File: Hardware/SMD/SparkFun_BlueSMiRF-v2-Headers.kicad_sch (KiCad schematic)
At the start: 38 parts, among them J1 Conn_01x06, Q1 NMOS_0.2A_50V, Q2 NMOS_0.2A_50V, SW1 SPST_Momentary_4.6x2.8mm, U1 ESP32-PICO-V3-02, U2 AP2112K-3.3

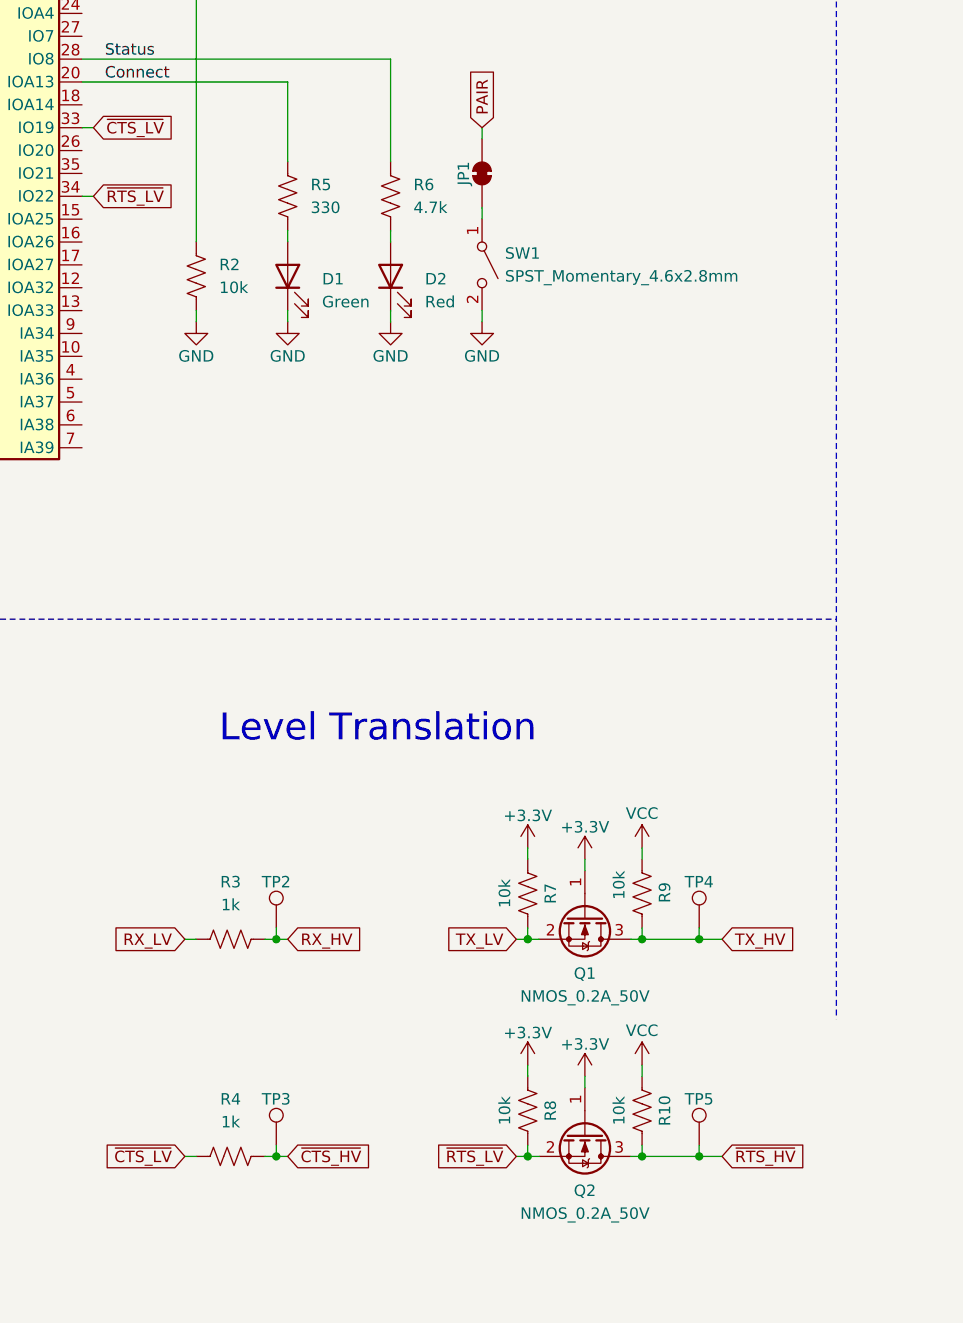
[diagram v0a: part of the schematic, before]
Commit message: Add 3D models
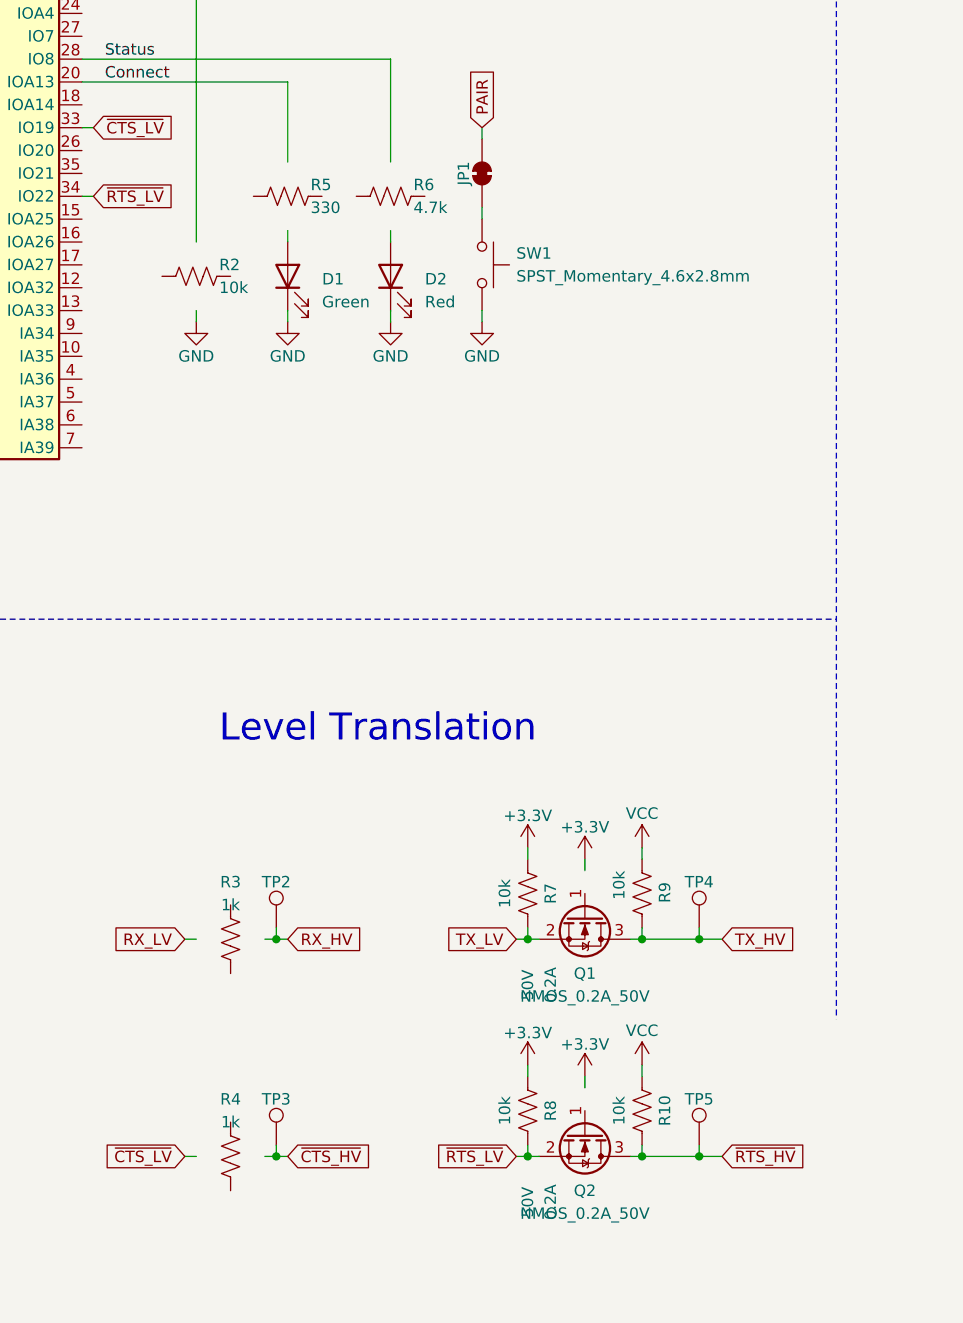
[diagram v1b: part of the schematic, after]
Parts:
- D1: footprint SparkFun-LED:LED_0603_1608Metric -> SparkFun-LED:LED_0603_1608Metric_Green
- D2: footprint SparkFun-LED:LED_0603_1608Metric -> SparkFun-LED:LED_0603_1608Metric_Red
- J1: footprint SparkFun-Connector:1X06-SMD_RA_MALE -> SparkFun-Connector:1x06_SMD_RA_Male
- JP1: footprint SparkFun-Jumper:SMT-JUMPER_2_NC_TRACE_SILK -> SparkFun-Jumper:Jumper_2_NC_Trace
- JP2: footprint SparkFun-Jumper:SMT-JUMPER_2_NO_SILK -> SparkFun-Jumper:Jumper_2_NO
- Q1, Q2: IMax (none) -> 0.2A; VMax (none) -> 50V
- SW1: footprint SparkFun-Switch:Momentary_SMD_4.6x2.8mm -> SparkFun-Switch:Push_SMD_4.6x2.8mm_h2.5mm; symbol SparkFun-Switch:SPST_Momentary_4.6x2.8mm -> SparkFun-Switch:SPST_Push_SMD_4.6x2.8mm_h2.5mm
- TP1: footprint SparkFun-Connector:1X01 -> SparkFun-Connector:1x01
- U1: footprint SparkFun-RF:ESP32-MINI -> SparkFun-RF:ESP32-PICO-MINI
- U2: Imax (none) -> 600mA; Iq (none) -> 55µA; VMax (none) -> 6V
- U3: footprint SparkFun-Aesthetic:ORDERING_INSTRUCTIONS -> SparkFun-Aesthetic:Ordering_Instructions
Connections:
- net +3.3V: no longer Q1.1 (G), Q2.1 (G)
- net Connect: no longer R5.1
- net GND: no longer R2.2
- net RX_HV: no longer R3.2
- net RX_LV: no longer R3.1
- net Status: no longer R6.1
- net ~{CTS_HV}: no longer R4.2
- net ~{CTS_LV}: no longer R4.1
- net at D1.2 (A): no longer R5.2
- net at U1.21 (IOA15): no longer R2.1
- net at R6.2: no longer D2.2 (A)

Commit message: Revert "Add 3D models"
This reverts commit f06ec004f059f8b2f723d6c27b798dd6a6ac20d5.
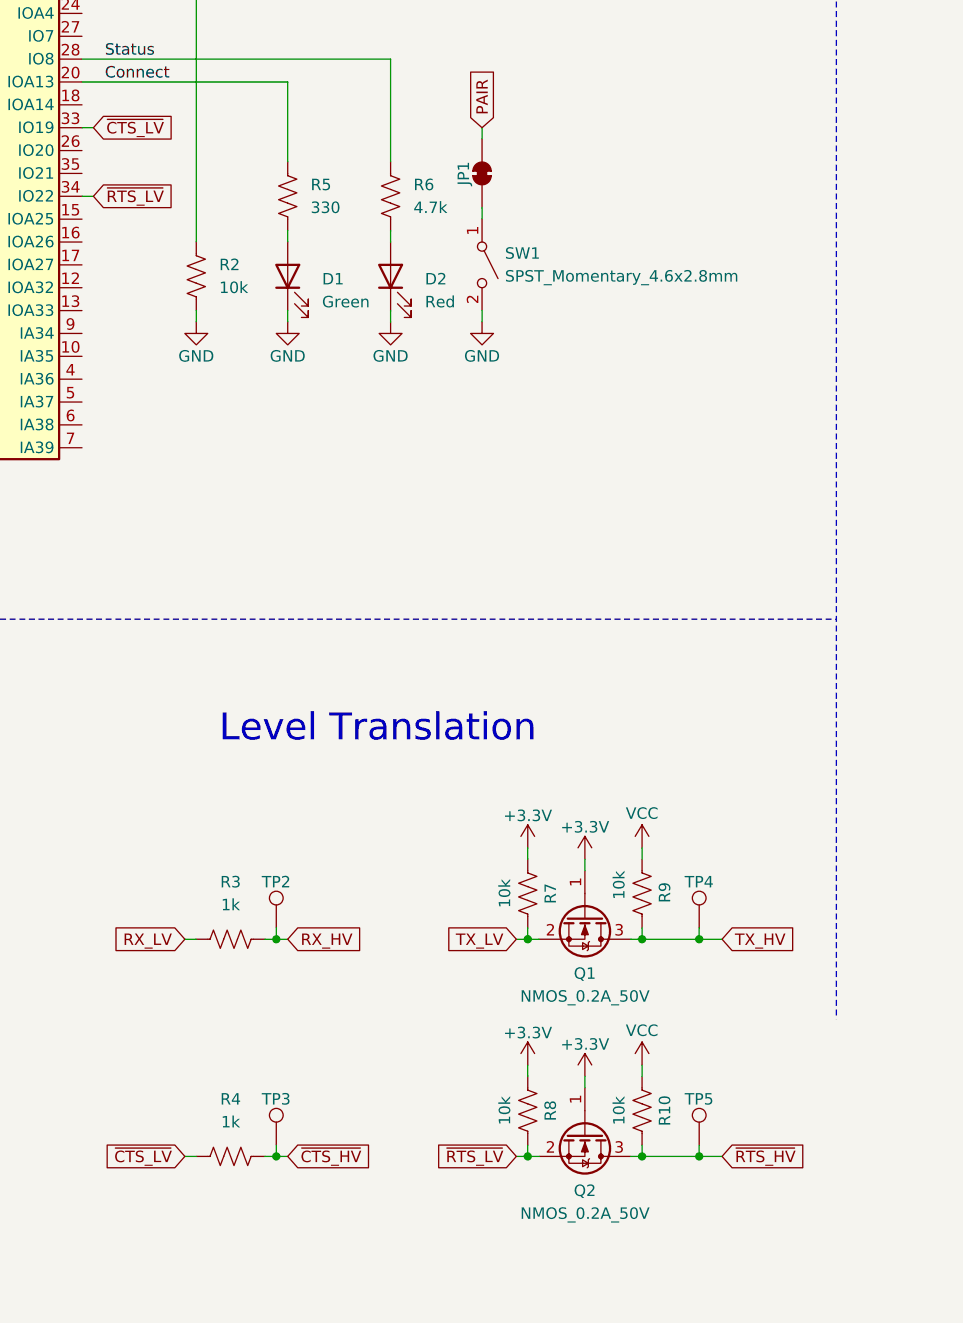
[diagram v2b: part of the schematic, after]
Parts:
- D1: footprint SparkFun-LED:LED_0603_1608Metric_Green -> SparkFun-LED:LED_0603_1608Metric
- D2: footprint SparkFun-LED:LED_0603_1608Metric_Red -> SparkFun-LED:LED_0603_1608Metric
- J1: footprint SparkFun-Connector:1x06_SMD_RA_Male -> SparkFun-Connector:1X06-SMD_RA_MALE
- JP1: footprint SparkFun-Jumper:Jumper_2_NC_Trace -> SparkFun-Jumper:SMT-JUMPER_2_NC_TRACE_SILK
- JP2: footprint SparkFun-Jumper:Jumper_2_NO -> SparkFun-Jumper:SMT-JUMPER_2_NO_SILK
- Q1, Q2: IMax 0.2A -> (none); VMax 50V -> (none)
- SW1: footprint SparkFun-Switch:Push_SMD_4.6x2.8mm_h2.5mm -> SparkFun-Switch:Momentary_SMD_4.6x2.8mm; symbol SparkFun-Switch:SPST_Push_SMD_4.6x2.8mm_h2.5mm -> SparkFun-Switch:SPST_Momentary_4.6x2.8mm
- TP1: footprint SparkFun-Connector:1x01 -> SparkFun-Connector:1X01
- U1: footprint SparkFun-RF:ESP32-PICO-MINI -> SparkFun-RF:ESP32-MINI
- U2: Imax 600mA -> (none); Iq 55µA -> (none); VMax 6V -> (none)
- U3: footprint SparkFun-Aesthetic:Ordering_Instructions -> SparkFun-Aesthetic:ORDERING_INSTRUCTIONS
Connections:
- net +3.3V: now also Q1.1 (G), Q2.1 (G)
- net Connect: now also R5.1
- net GND: now also R2.2
- net RX_HV: now also R3.2
- net RX_LV: now also R3.1
- net Status: now also R6.1
- net ~{CTS_HV}: now also R4.2
- net ~{CTS_LV}: now also R4.1
- net at D1.2 (A): now also R5.2
- net at U1.21 (IOA15): now also R2.1
- net at R6.2: now also D2.2 (A)
